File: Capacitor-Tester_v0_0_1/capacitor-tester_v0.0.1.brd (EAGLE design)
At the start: 67 x 40 mm, 34 parts, among them IC1 AD8397ARDZ, IC2 DAC6571IDBVT, IC3 AD8531ARZ, IC4 MC34063EBD-TR, J1 DS1044-140G, J2 250-103, J3 USB4125-GF-A-0190_REVA2, U1 AD5933, Y1 LFSPXO018034

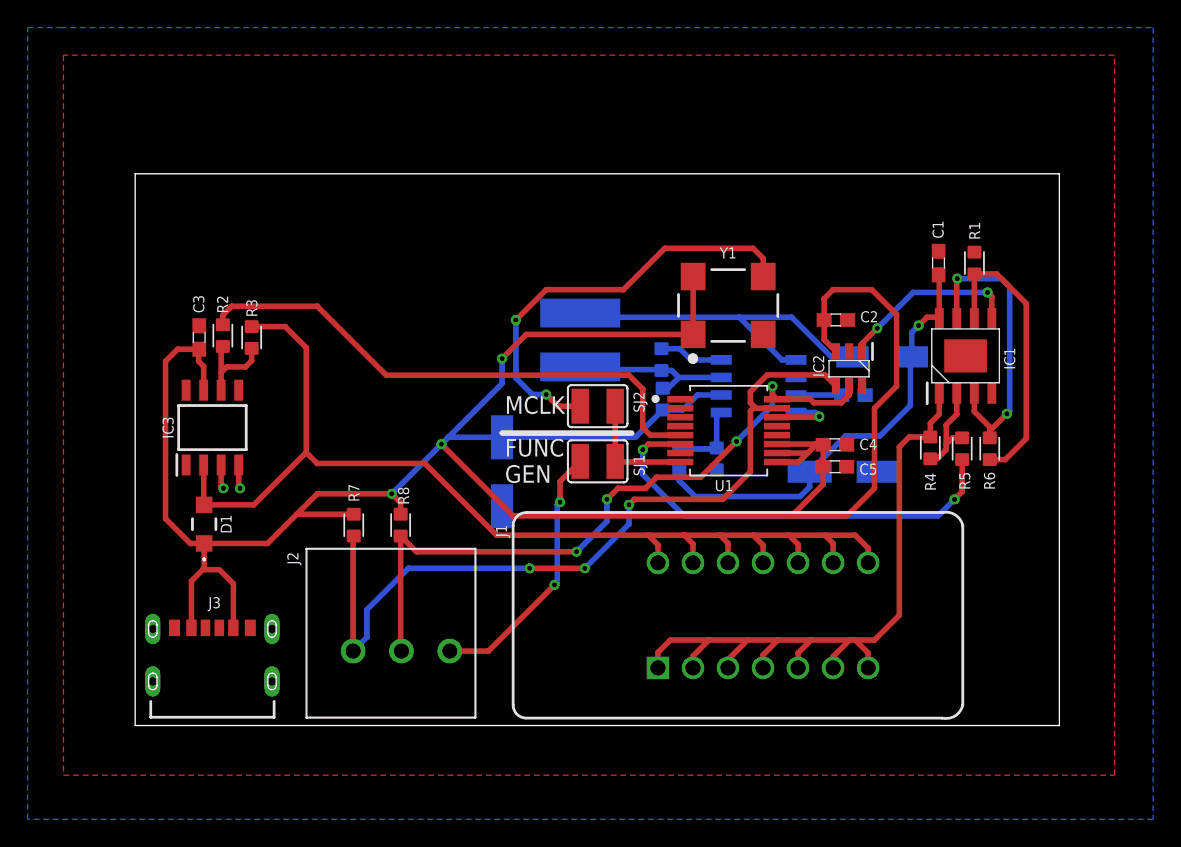
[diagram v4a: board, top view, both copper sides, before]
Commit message: IN PROGRESS - v0.0.1 new component layout
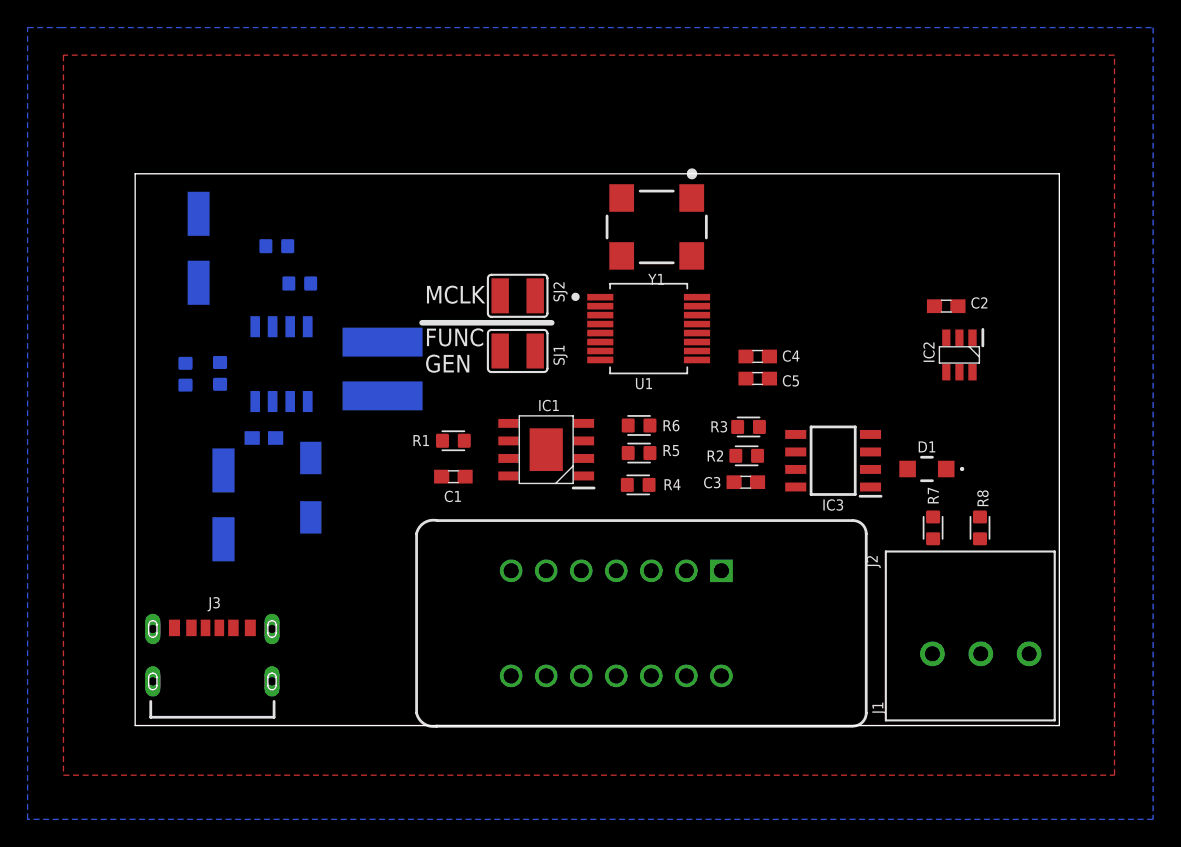
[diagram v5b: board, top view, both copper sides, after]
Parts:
- moved D1 52.6 mm to (57.4, 18.6), turned to 180 degrees
- moved C6 45.1 mm to (6.40, 16.0), turned to 90 degrees
- moved IC3 45.1 mm to (50.6, 19.2), turned to 180 degrees
- moved C8 42.9 mm to (9.33, 20.8), turned to 0 degrees
- moved D2 42.5 mm to (12.7, 17.2), turned to 90 degrees
- moved J2 42.0 mm to (57.8, 5.20)
- moved R7 42.0 mm to (57.8, 14.3)
- moved R8 42.0 mm to (61.2, 14.3)
- moved C3 41.0 mm to (44.3, 17.6), turned to 180 degrees
- moved R1 39.9 mm to (23.1, 20.6), turned to 180 degrees
- moved R2 39.0 mm to (44.3, 19.6), turned to 0 degrees
- moved C1 38.4 mm to (23.1, 18.0), turned to 180 degrees
- moved R3 36.6 mm to (44.5, 21.6), turned to 180 degrees
- moved R10 36.5 mm to (6.15, 25.5)
- moved R9 36.3 mm to (3.65, 25.5)
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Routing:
- net +5V: track 180.2 -> 0.00 mm, vias 3 -> 0
- net Z_OUT: track 82.4 -> 0.00 mm
- net SDA: track 59.3 -> 0.00 mm, vias 3 -> 0
- net UZA_OUT: track 52.8 -> 0.00 mm
- net SCL: track 49.8 -> 0.00 mm, vias 4 -> 0
- net VIN: track 39.6 -> 0.00 mm
- net +12V: track 32.3 -> 0.00 mm, vias 1 -> 0
- net VOUT: track 32.1 -> 0.00 mm, vias 2 -> 0
- net MCLK: track 31.4 -> 0.00 mm, vias 2 -> 0
- net N$5: track 26.4 -> 0.00 mm
- net UZB_OUT: track 22.2 -> 0.00 mm, vias 2 -> 0
- net N$13: track 21.0 -> 0.00 mm
- net FUNC_GEN: track 19.3 -> 0.00 mm, vias 2 -> 0
- net DAC_OUT: track 13.2 -> 0.00 mm, vias 2 -> 0
- net N$11: track 12.0 -> 0.00 mm
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
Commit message: IN PROGRESS - v0.0.1 routing traces
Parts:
- moved R11 18.9 mm to (9.67, 15.8), flipped to the top, turned to 0 degrees
- moved C6 18.6 mm to (5.80, 34.6), flipped to the top, turned to 270 degrees
- moved C7 18.6 mm to (4.00, 16.0), flipped to the top, turned to 90 degrees
- moved D2 16.1 mm to (12.1, 33.4), flipped to the top, turned to 270 degrees
- moved D1 15.4 mm to (42.0, 19.4), turned to 90 degrees
- moved R12 13.5 mm to (11.3, 18.6), flipped to the top, turned to 180 degrees
- moved C3 10.6 mm to (54.1, 21.6), turned to 0 degrees
- moved R3 10.3 mm to (53.9, 17.6), turned to 0 degrees
- moved R2 9.74 mm to (54.1, 19.6), turned to 180 degrees
- moved C8 8.93 mm to (8.73, 29.8), flipped to the top, turned to 180 degrees
- moved C2 3.40 mm to (60.4, 27.4)
- moved IC2 3.10 mm to (60.6, 23.9)
- moved IC3 2.91 mm to (47.8, 20.0), turned to 0 degrees
- moved IC4 1.90 mm to (10.0, 24.4), flipped to the top, turned to 270 degrees
- moved L1 1.25 mm to (17.3, 24.8), flipped to the top, turned to 0 degrees
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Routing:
- net +5V: track 0.00 -> 107.3 mm
- net +12V: track 0.00 -> 51.4 mm, vias 0 -> 2
- net UZA_OUT: track 0.00 -> 18.5 mm
- net Z_OUT: track 0.00 -> 18.4 mm
- net N$11: track 0.00 -> 15.9 mm
- net N$5: track 0.00 -> 12.6 mm
- net MCLK: track 0.00 -> 11.1 mm
- net SDA: track 0.00 -> 9.69 mm
- net SCL: track 0.00 -> 9.61 mm
- net N$6: track 0.00 -> 8.99 mm
- net N$7: track 0.00 -> 7.10 mm
- net N$4: track 0.00 -> 5.93 mm
- net N$1: track 0.00 -> 4.84 mm
- net UZB_OUT: track 0.00 -> 3.69 mm
- net N$8: track 0.00 -> 3.31 mm
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
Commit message: IN PROGRESS - Trace routing
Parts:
- moved C2 0.20 mm to (60.4, 27.6)
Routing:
- net FUNC_GEN: track 0.00 -> 49.8 mm, vias 0 -> 1
- net DAC_OUT: track 0.00 -> 45.3 mm, vias 0 -> 4
- net +5V: track 107.3 -> 143.8 mm, vias 0 -> 4
- net SCL: track 9.61 -> 43.6 mm, vias 0 -> 2
- net SDA: track 9.69 -> 41.1 mm, vias 0 -> 2
- net Z_OUT: track 18.4 -> 47.2 mm
- net N$13: track 2.43 -> 18.5 mm, vias 0 -> 2
- net GND: track 0.00 -> 14.9 mm, vias 0 -> 3
- net UZB_OUT: track 3.69 -> 15.5 mm, vias 0 -> 2
- net VOUT: track 0.00 -> 11.7 mm, vias 0 -> 2
- net UZA_OUT: track 18.5 -> 25.5 mm

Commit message: IN PROGRESS - Finished routing traces
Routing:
- net VIN: track 0.00 -> 29.9 mm, vias 0 -> 2
- net GND: track 14.9 -> 16.7 mm, vias 3 -> 4
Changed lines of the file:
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@@
 <wire x1="40.731" y1="29.754" x2="42.246" y2="29.754" width="0.4064" layer="1"/>
 <wire x1="42.246" y1="29.754" x2="42.896" y2="29.104" width="0.4064" layer="1"/>
+<wire x1="54.981" y1="21.554" x2="55.646" y2="21.554" width="0.4064" layer="1"/>
+<wire x1="55.646" y1="21.554" x2="56.4" y2="20.8" width="0.4064" layer="1"/>
+<via x="56.4" y="20.8" extent="1-16" drill="0.35"/>
 </signal>
 <signal name="+5V">
@@
 <contactref element="U1" pad="5"/>
 <contactref element="R2" pad="1"/>
-<wire x1="33.721" y1="28.454" x2="54.859" y2="19.646" width="0" layer="19" extent="1-1"/>
+<wire x1="54.859" y1="19.646" x2="57.354" y2="19.646" width="0.4064" layer="1"/>
+<wire x1="57.354" y1="19.646" x2="57.4" y2="19.6" width="0.4064" layer="1"/>
+<via x="57.4" y="19.6" extent="1-16" drill="0.35"/>
+<wire x1="33.721" y1="28.454" x2="36.546" y2="28.454" width="0.4064" layer="1"/>
+<wire x1="36.546" y1="28.454" x2="37" y2="28" width="0.4064" layer="1"/>
+<via x="37" y="28" extent="1-16" drill="0.35"/>
+<wire x1="37" y1="28" x2="42" y2="28" width="0.4064" layer="16"/>
+<wire x1="50.4" y1="19.6" x2="57.4" y2="19.6" width="0.4064" layer="16"/>
+<wire x1="42" y1="28" x2="50.4" y2="19.6" width="0.4064" layer="16"/>
 </signal>
 <signal name="VOUT">
@@
 <contactref element="R10" pad="1"/>
 <contactref element="IC4" pad="5"/>
-<wire x1="5.554" y1="24.2" x2="5.554" y2="24.279" width="0.4064" layer="1"/>
+<wire x1="8.095" y1="21.688" x2="6.512" y2="21.688" width="0.6096" layer="1"/>
 <wire x1="3.046" y1="24.341" x2="5.492" y2="24.341" width="0.6096" layer="1"/>
-<wire x1="5.554" y1="24.279" x2="5.6" y2="24.233" width="0.6096" layer="1"/>
-<wire x1="6.512" y1="21.688" x2="8.095" y2="21.688" width="0.6096" layer="1"/>
-<wire x1="5.6" y1="24.233" x2="5.6" y2="22.6" width="0.6096" layer="1"/>
-<wire x1="5.6" y1="22.6" x2="6.512" y2="21.688" width="0.6096" layer="1"/>
-<wire x1="5.554" y1="24.279" x2="5.492" y2="24.341" width="0" layer="19" extent="1-1"/>
+<wire x1="5.492" y1="24.341" x2="5.554" y2="24.279" width="0.6096" layer="1"/>
+<wire x1="5.492" y1="22.708" x2="5.492" y2="24.341" width="0.6096" layer="1"/>
+<wire x1="6.512" y1="21.688" x2="5.492" y2="22.708" width="0.6096" layer="1"/>
 </signal>
 <signal name="N$11">
